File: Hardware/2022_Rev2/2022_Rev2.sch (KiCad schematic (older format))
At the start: 36 parts

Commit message: molex pins
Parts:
- added Conn? (x2): Molex_SL_10, symbol MRDT_Connectors:Molex_SL_10
- added Conn? (x2): Molex_SL_02, symbol MRDT_Connectors:Molex_SL_02
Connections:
- net labels added: TeensyMolexPins
- net labels removed: Teensy
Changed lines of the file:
@@
 $Descr A4 11693 8268
 encoding utf-8
-Sheet 1 5
+Sheet 1 4
 Title ""
 Date ""
@@
 	1    0    0    -1
 $EndComp
-Text GLabel 2000 1050 0    50   Input ~ 0
-Current_Sense_Drive
-Text GLabel 2000 1450 0    50   Input ~ 0
-Current_Sense_Nav
-Wire Wire Line
-	2000 1050 2150 1050
-Wire Wire Line
-	2150 1450 2000 1450
-Text GLabel 4600 1050 2    50   Output ~ 0
-Driver_Drive
-Wire Wire Line
-	4450 1050 4600 1050
-Text GLabel 4600 1450 2    50   Output ~ 0
-Driver_Nav
-Wire Wire Line
-	4450 1450 4600 1450
 Wire Notes Line
 	500  500  5350 500
 Text Label 450  2500 0    315  Italic 63
-Teensy
+TeensyMolexPins
 Wire Notes Line
 	500  2500 5350 2500
@@
 Text Label 7100 7050 0    157  Italic 31
 "Rev4"
-$Sheet
-S 2150 600  2300 1800
-U 62118F7B
-F0 "TEENSY" 50
-F1 "TEENSY.sch" 50
-F2 "Current_Sense_Drive" I L 2150 1050 50
-F3 "Current_Sense_Nav" I L 2150 1450 50
-F4 "Driver_Drive" O R 4450 1050 50
-F5 "Driver_Nav" O R 4450 1450 50
-F6 "Current_Sense_BBB" I L 2150 750 50
-F7 "Current_Sense_Multi" I L 2150 1350 50
-F8 "Current_Sense_Cam2" I L 2150 950 50
-F9 "Current_Sense_Cam1" I L 2150 850 50
-F10 "Driver_BBB" O R 4450 750 50
-F11 "Driver_Multi" O R 4450 1350 50
-F12 "Driver_GimAct" O R 4450 1150 50
-F13 "Driver_Cam1" O R 4450 850 50
-F14 "Driver_Cam2" O R 4450 950 50
-F15 "Current_Sense_GimAct" I L 2150 1150 50
-F16 "Driver_GimLog" O R 4450 1250 50
-F17 "Driver_NetSwitch" O R 4450 1550 50
-F18 "Driver_AuxLog" O R 4450 650 50
-F19 "Driver_SciLog" O R 4450 1750 50
-F20 "Driver_SciAct" O R 4450 1650 50
-F21 "Current_Sense_GimLog" I L 2150 1250 50
-F22 "Current_Sense_NetSwitch" I L 2150 1550 50
-F23 "Current_Sense_SciAct" I L 2150 1650 50
-F24 "Current_Sense_SciLog" I L 2150 1750 50
-F25 "Current_Sense_AuxLog" I L 2150 650 50
-$EndSheet
-Text GLabel 2000 650  0    50   Input ~ 0
-Current_Sense_AuxLog
-Wire Wire Line
-	2000 650  2150 650
-Text GLabel 2000 750  0    50   Input ~ 0
-Current_Sense_BBB
-Wire Wire Line
-	2000 750  2150 750
-Text GLabel 2000 850  0    50   Input ~ 0
-Current_Sense_Cam1
-Wire Wire Line
-	2000 850  2150 850
-Text GLabel 2000 950  0    50   Input ~ 0
-Current_Sense_Cam2
-Wire Wire Line
-	2000 950  2150 950
-Text GLabel 2000 1150 0    50   Input ~ 0
-Current_Sense_GimAct
-Wire Wire Line
-	2000 1150 2150 1150
-Text GLabel 2000 1250 0    50   Input ~ 0
-Current_Sense_GimLog
-Wire Wire Line
-	2000 1250 2150 1250
-Text GLabel 2000 1350 0    50   Input ~ 0
-Current_Sense_Multi
-Wire Wire Line
-	2000 1350 2150 1350
-Text GLabel 2000 1550 0    50   Input ~ 0
-Current_Sense_NetSwitch
-Wire Wire Line
-	2000 1550 2150 1550
-Text GLabel 2000 1650 0    50   Input ~ 0
-Current_Sense_SciAct
-Wire Wire Line
-	2000 1650 2150 1650
-Text GLabel 2000 1750 0    50   Input ~ 0
-Current_Sense_SciLog
-Wire Wire Line
-	2000 1750 2150 1750
-Text GLabel 4600 650  2    50   Output ~ 0
-Driver_AuxLog
-Wire Wire Line
-	4450 650  4600 650
-Text GLabel 4600 750  2    50   Output ~ 0
-Driver_BBB
-Wire Wire Line
-	4450 750  4600 750
-Text GLabel 4600 850  2    50   Output ~ 0
-Driver_Cam1
-Wire Wire Line
-	4450 850  4600 850
-Text GLabel 4600 950  2    50   Output ~ 0
-Driver_Cam2
-Wire Wire Line
-	4450 950  4600 950
-Text GLabel 4600 1150 2    50   Output ~ 0
-Driver_GimAct
-Wire Wire Line
-	4450 1150 4600 1150
-Text GLabel 4600 1250 2    50   Output ~ 0
-Driver_GimLog
-Wire Wire Line
-	4450 1250 4600 1250
-Text GLabel 4600 1350 2    50   Output ~ 0
-Driver_Multi
-Wire Wire Line
-	4450 1350 4600 1350
-Text GLabel 4600 1550 2    50   Output ~ 0
-Driver_NetSwitch
-Wire Wire Line
-	4450 1550 4600 1550
-Text GLabel 4600 1650 2    50   Output ~ 0
-Driver_SciAct
-Wire Wire Line
-	4450 1650 4600 1650
-Text GLabel 4600 1750 2    50   Output ~ 0
-Driver_SciLog
-Wire Wire Line
-	4450 1750 4600 1750
 Text GLabel 5950 1500 0    50   Input ~ 0
 Driver_Drive
@@
 Connection ~ 10150 6500
 Connection ~ 10400 6500
+$Comp
+L MRDT_Connectors:Molex_SL_10 Conn?
+U 1 1 622C6D4E
+P 2300 1550
+F 0 "Conn?" H 2428 2108 60  0000 L CNN
+F 1 "Molex_SL_10" H 2428 2002 60  0000 L CNN
+F 2 "" H 2300 2050 60  0001 C CNN
+F 3 "" H 2300 2050 60  0001 C CNN
+	1    2300 1550
+	1    0    0    -1
+$EndComp
+$Comp
+L MRDT_Connectors:Molex_SL_02 Conn?
+U 1 1 622C7AC7
+P 2300 1750
+F 0 "Conn?" H 2428 1908 60  0000 L CNN
+F 1 "Molex_SL_02" H 2428 1802 60  0000 L CNN
+F 2 "" H 2300 1650 60  0001 C CNN
+F 3 "" H 2300 1650 60  0001 C CNN
+	1    2300 1750
+	1    0    0    -1
+$EndComp
+$Comp
+L MRDT_Connectors:Molex_SL_10 Conn?
+U 1 1 622C9F32
+P 3800 1550
+F 0 "Conn?" H 3928 2108 60  0000 L CNN
+F 1 "Molex_SL_10" H 3928 2002 60  0000 L CNN
+F 2 "" H 3800 2050 60  0001 C CNN
+F 3 "" H 3800 2050 60  0001 C CNN
+	1    3800 1550
+	-1   0    0    -1
+$EndComp
+$Comp
+L MRDT_Connectors:Molex_SL_02 Conn?
+U 1 1 622C9F38
+P 3800 1750
+F 0 "Conn?" H 3928 1908 60  0000 L CNN
+F 1 "Molex_SL_02" H 3928 1802 60  0000 L CNN
+F 2 "" H 3800 1650 60  0001 C CNN
+F 3 "" H 3800 1650 60  0001 C CNN
+	1    3800 1750
+	-1   0    0    -1
+$EndComp
+Text GLabel 1950 1000 0    50   Input ~ 0
+Current_Sense_Drive
+Text GLabel 1950 1400 0    50   Input ~ 0
+Current_Sense_Nav
+Wire Wire Line
+	1950 1000 2100 1000
+Wire Wire Line
+	2100 1400 1950 1400
+Text GLabel 1950 600  0    50   Input ~ 0
+Current_Sense_AuxLog
+Wire Wire Line
+	1950 600  2100 600
+Text GLabel 1950 700  0    50   Input ~ 0
+Current_Sense_BBB
+Wire Wire Line
+	1950 700  2100 700
+Text GLabel 1950 800  0    50   Input ~ 0
+Current_Sense_Cam1
+Wire Wire Line
+	1950 800  2100 800
+Text GLabel 1950 900  0    50   Input ~ 0
+Current_Sense_Cam2
+Wire Wire Line
+	1950 900  2100 900
+Text GLabel 1950 1100 0    50   Input ~ 0
+Current_Sense_GimAct
+Wire Wire Line
+	1950 1100 2100 1100
+Text GLabel 1950 1200 0    50   Input ~ 0
+Current_Sense_GimLog
+Wire Wire Line
+	1950 1200 2100 1200
+Text GLabel 1950 1300 0    50   Input ~ 0
+Current_Sense_Multi
+Wire Wire Line
+	1950 1300 2100 1300
+Text GLabel 1950 1500 0    50   Input ~ 0
+Current_Sense_NetSwitch
+Wire Wire Line
+	1950 1500 2100 1500
+Text GLabel 1950 1600 0    50   Input ~ 0
+Current_Sense_SciAct
+Wire Wire Line
+	1950 1600 2100 1600
+Text GLabel 1950 1700 0    50   Input ~ 0
+Current_Sense_SciLog
+Wire Wire Line
+	1950 1700 2100 1700
+Text GLabel 4150 1000 2    50   Output ~ 0
+Driver_Drive
+Wire Wire Line
+	4000 1000 4150 1000
+Text GLabel 4150 1400 2    50   Output ~ 0
+Driver_Nav
+Wire Wire Line
+	4000 1400 4150 1400
+Text GLabel 4150 600  2    50   Output ~ 0
+Driver_AuxLog
+Wire Wire Line
+	4000 600  4150 600
+Text GLabel 4150 700  2    50   Output ~ 0
+Driver_BBB
+Wire Wire Line
+	4000 700  4150 700
+Text GLabel 4150 800  2    50   Output ~ 0
+Driver_Cam1
+Wire Wire Line
+	4000 800  4150 800
+Text GLabel 4150 900  2    50   Output ~ 0
+Driver_Cam2
+Wire Wire Line
+	4000 900  4150 900
+Text GLabel 4150 1100 2    50   Output ~ 0
+Driver_GimAct
+Wire Wire Line
+	4000 1100 4150 1100
+Text GLabel 4150 1200 2    50   Output ~ 0
+Driver_GimLog
+Wire Wire Line
+	4000 1200 4150 1200
+Text GLabel 4150 1300 2    50   Output ~ 0
+Driver_Multi
+Wire Wire Line
+	4000 1300 4150 1300
+Text GLabel 4150 1500 2    50   Output ~ 0
+Driver_NetSwitch
+Wire Wire Line
+	4000 1500 4150 1500
+Text GLabel 4150 1600 2    50   Output ~ 0
+Driver_SciAct
+Wire Wire Line
+	4000 1600 4150 1600
+Text GLabel 4150 1700 2    50   Output ~ 0
+Driver_SciLog
+Wire Wire Line
+	4000 1700 4150 1700
 $EndSCHEMATC

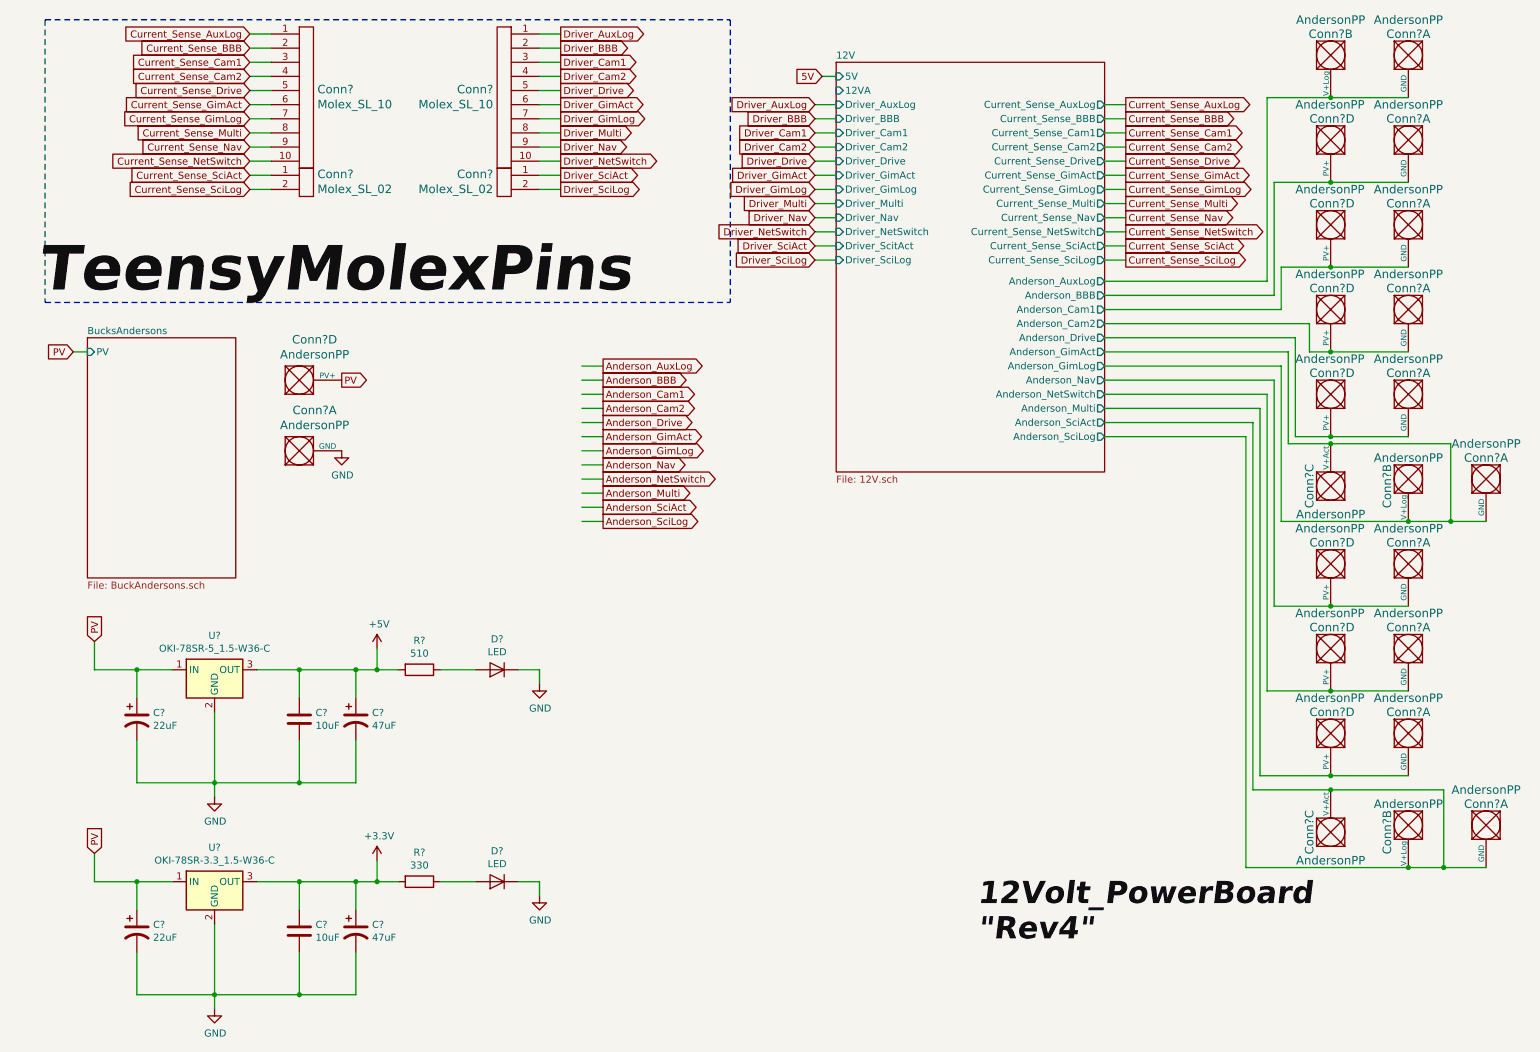
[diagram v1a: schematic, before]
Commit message: removed scilog/sciact
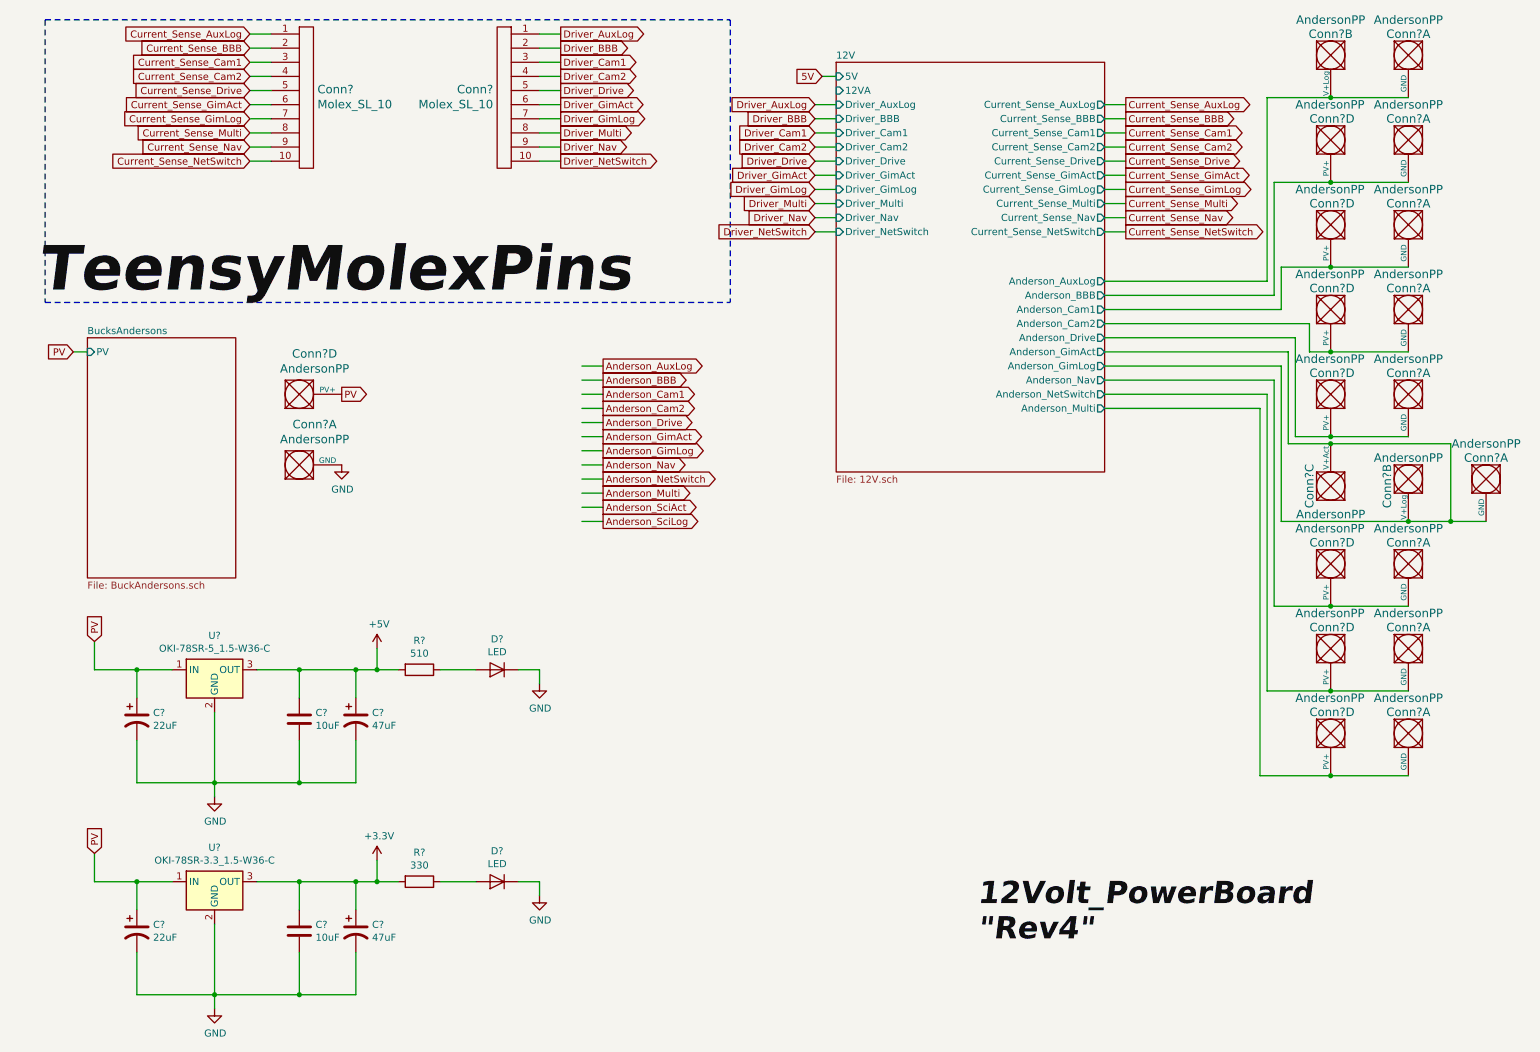
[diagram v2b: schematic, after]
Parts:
- removed Conn? (x2): Molex_SL_02, symbol MRDT_Connectors:Molex_SL_02
- removed Conn? (x3): AndersonPP, symbol MRDT_Connectors:AndersonPP
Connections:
- net labels removed: Current_Sense_SciAct, Current_Sense_SciLog, Driver_SciAct, Driver_SciLog
- wire segments 158 -> 140
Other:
- moved on the sheet: Conn?A, Conn?D
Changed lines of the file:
@@
 L 2022_Rev2-rescue:AndersonPP-MRDT_Connectors Conn?
 U 4 1 62120188
-P 2200 3150
+P 2200 3250
 AR Path="/62118E70/62120188" Ref="Conn?"  Part="4"
 AR Path="/62120188" Ref="Conn?"  Part="4"
-F 0 "Conn?" H 2408 3537 60  0000 C CNN
-F 1 "AndersonPP" H 2408 3431 60  0000 C CNN
-F 2 "" H 2050 2600 60  0001 C CNN
-F 3 "" H 2050 2600 60  0001 C CNN
-	4    2200 3150
+F 0 "Conn?" H 2408 3637 60  0000 C CNN
+F 1 "AndersonPP" H 2408 3531 60  0000 C CNN
+F 2 "" H 2050 2700 60  0001 C CNN
+F 3 "" H 2050 2700 60  0001 C CNN
+	4    2200 3250
 	1    0    0    -1
 $EndComp
@@
 L 2022_Rev2-rescue:AndersonPP-MRDT_Connectors Conn?
 U 1 1 6212018E
-P 2200 3650
+P 2200 3750
 AR Path="/62118E70/6212018E" Ref="Conn?"  Part="1"
 AR Path="/6212018E" Ref="Conn?"  Part="1"
-F 0 "Conn?" H 2408 4037 60  0000 C CNN
-F 1 "AndersonPP" H 2408 3931 60  0000 C CNN
-F 2 "" H 2050 3100 60  0001 C CNN
-F 3 "" H 2050 3100 60  0001 C CNN
-	1    2200 3650
+F 0 "Conn?" H 2408 4137 60  0000 C CNN
+F 1 "AndersonPP" H 2408 4031 60  0000 C CNN
+F 2 "" H 2050 3200 60  0001 C CNN
+F 3 "" H 2050 3200 60  0001 C CNN
+	1    2200 3750
 	1    0    0    -1
 $EndComp
@@
 L power:GND #PWR?
 U 1 1 62120194
-P 2600 3550
+P 2600 3650
 AR Path="/62118E70/62120194" Ref="#PWR?"  Part="1"
 AR Path="/62120194" Ref="#PWR?"  Part="1"
-F 0 "#PWR?" H 2600 3300 50  0001 C CNN
-F 1 "GND" H 2605 3377 50  0000 C CNN
-F 2 "" H 2600 3550 50  0001 C CNN
-F 3 "" H 2600 3550 50  0001 C CNN
-	1    2600 3550
-	1    0    0    -1
-$EndComp
-Text GLabel 2600 3050 2    50   Output ~ 0
+F 0 "#PWR?" H 2600 3400 50  0001 C CNN
+F 1 "GND" H 2605 3477 50  0000 C CNN
+F 2 "" H 2600 3650 50  0001 C CNN
+F 3 "" H 2600 3650 50  0001 C CNN
+	1    2600 3650
+	1    0    0    -1
+$EndComp
+Text GLabel 2600 3150 2    50   Output ~ 0
 PV
 Text GLabel 850  4900 1    50   Input ~ 0
@@
 Wire Wire Line
 	6100 2000 5950 2000
-Text GLabel 5950 2100 0    50   Input ~ 0
-Driver_SciAct
-Wire Wire Line
-	6100 2100 5950 2100
-Text GLabel 5950 2200 0    50   Input ~ 0
-Driver_SciLog
-Wire Wire Line
-	6100 2200 5950 2200
 Text GLabel 8150 1500 2    50   Output ~ 0
 Current_Sense_Drive
@@
 Wire Wire Line
 	8150 2000 8000 2000
-Text GLabel 8150 2100 2    50   Output ~ 0
-Current_Sense_SciAct
-Wire Wire Line
-	8150 2100 8000 2100
-Text GLabel 8150 2200 2    50   Output ~ 0
-Current_Sense_SciLog
-Wire Wire Line
-	8150 2200 8000 2200
 Text GLabel 4450 2950 2    50   Output ~ 0
 Anderson_AuxLog
@@
 Wire Wire Line
 	4450 3850 4300 3850
-Text GLabel 4450 3950 2    50   Output ~ 0
-Anderson_SciAct
-Wire Wire Line
-	4450 3950 4300 3950
-Text GLabel 4450 4050 2    50   Output ~ 0
-Anderson_SciLog
-Wire Wire Line
-	4450 4050 4300 4050
 $Comp
 L MRDT_Connectors:AndersonPP Conn?
@@
 F9 "Anderson_GimAct" O R 8000 2850 50
 F10 "Driver_GimAct" I L 6100 1600 50
-F11 "Current_Sense_SciAct" O R 8000 2100 50
-F12 "Anderson_SciAct" O R 8000 3350 50
-F13 "Driver_ScitAct" I L 6100 2100 50
-F14 "Current_Sense_Cam1" O R 8000 1300 50
-F15 "Current_Sense_Cam2" O R 8000 1400 50
-F16 "Current_Sense_GimLog" O R 8000 1700 50
-F17 "Current_Sense_Multi" O R 8000 1800 50
-F18 "Current_Sense_NetSwitch" O R 8000 2000 50
-F19 "Current_Sense_SciLog" O R 8000 2200 50
-F20 "Anderson_BBB" O R 8000 2450 50
-F21 "Anderson_Cam1" O R 8000 2550 50
-F22 "Anderson_Cam2" O R 8000 2650 50
-F23 "Anderson_GimLog" O R 8000 2950 50
-F24 "Anderson_Multi" O R 8000 3250 50
-F25 "Anderson_Nav" O R 8000 3050 50
-F26 "Anderson_NetSwitch" O R 8000 3150 50
-F27 "Anderson_SciLog" O R 8000 3450 50
-F28 "Driver_BBB" I L 6100 1200 50
-F29 "Driver_Cam1" I L 6100 1300 50
-F30 "Driver_Cam2" I L 6100 1400 50
-F31 "Driver_GimLog" I L 6100 1700 50
-F32 "Driver_Multi" I L 6100 1800 50
-F33 "Driver_NetSwitch" I L 6100 2000 50
-F34 "Driver_SciLog" I L 6100 2200 50
-F35 "12VA" I L 6100 1000 50
-F36 "Current_Sense_AuxLog" O R 8000 1100 50
-F37 "Current_Sense_BBB" O R 8000 1200 50
-F38 "Anderson_AuxLog" O R 8000 2350 50
-F39 "Driver_AuxLog" I L 6100 1100 50
+F11 "Current_Sense_Cam1" O R 8000 1300 50
+F12 "Current_Sense_Cam2" O R 8000 1400 50
+F13 "Current_Sense_GimLog" O R 8000 1700 50
+F14 "Current_Sense_Multi" O R 8000 1800 50
+F15 "Current_Sense_NetSwitch" O R 8000 2000 50
+F16 "Anderson_BBB" O R 8000 2450 50
+F17 "Anderson_Cam1" O R 8000 2550 50
+F18 "Anderson_Cam2" O R 8000 2650 50
+F19 "Anderson_GimLog" O R 8000 2950 50
+F20 "Anderson_Multi" O R 8000 3250 50
+F21 "Anderson_Nav" O R 8000 3050 50
+F22 "Anderson_NetSwitch" O R 8000 3150 50
+F23 "Driver_BBB" I L 6100 1200 50
+F24 "Driver_Cam1" I L 6100 1300 50
+F25 "Driver_Cam2" I L 6100 1400 50
+F26 "Driver_GimLog" I L 6100 1700 50
+F27 "Driver_Multi" I L 6100 1800 50
+F28 "Driver_NetSwitch" I L 6100 2000 50
+F29 "12VA" I L 6100 1000 50
+F30 "Current_Sense_AuxLog" O R 8000 1100 50
+F31 "Current_Sense_BBB" O R 8000 1200 50
+F32 "Anderson_AuxLog" O R 8000 2350 50
+F33 "Driver_AuxLog" I L 6100 1100 50
 $EndSheet
 Wire Wire Line
@@
 Connection ~ 10150 4050
 Connection ~ 10450 4050
-$Comp
-L MRDT_Connectors:AndersonPP Conn?
-U 1 1 626D966C
-P 10600 6100
-F 0 "Conn?" V 10550 6200 60  0000 C CNN
-F 1 "AndersonPP" V 10450 6200 60  0000 C CNN
-F 2 "" H 10450 5550 60  0001 C CNN
-F 3 "" H 10450 5550 60  0001 C CNN
-	1    10600 6100
-	0    1    1    0
-$EndComp
-$Comp
-L MRDT_Connectors:AndersonPP Conn?
-U 3 1 626D9672
-P 9700 6350
-F 0 "Conn?" H 9800 6600 60  0000 C CNN
-F 1 "AndersonPP" V 9600 6450 60  0000 C CNN
-F 2 "" H 9550 5800 60  0001 C CNN
-F 3 "" H 9550 5800 60  0001 C CNN
-	3    9700 6350
-	0    -1   -1   0
-$EndComp
-$Comp
-L MRDT_Connectors:AndersonPP Conn?
-U 2 1 626D9678
-P 10050 6100
-F 0 "Conn?" H 10200 6050 60  0000 C CNN
-F 1 "AndersonPP" V 10000 6200 60  0000 C CNN
-F 2 "" H 9900 5550 60  0001 C CNN
-F 3 "" H 9900 5550 60  0001 C CNN
-	2    10050 6100
-	0    1    1    0
-$EndComp
 Wire Wire Line
 	8000 3050 9200 3050
@@
 Wire Wire Line
 	9600 5850 10150 5850
-Wire Wire Line
-	8000 3350 9050 3350
-Wire Wire Line
-	9050 3350 9050 5950
-Wire Wire Line
-	9050 5950 9600 5950
-Wire Wire Line
-	8000 3450 9000 3450
-Wire Wire Line
-	9000 3450 9000 6500
-Wire Wire Line
-	9000 6500 10150 6500
-Wire Wire Line
-	9600 5950 10400 5950
-Wire Wire Line
-	10400 5950 10400 6500
-Wire Wire Line
-	10400 6500 10700 6500
-Connection ~ 9600 5950
-Wire Wire Line
-	10150 6500 10400 6500
-Connection ~ 10150 6500
-Connection ~ 10400 6500
 $Comp
 L MRDT_Connectors:Molex_SL_10 Conn?
@@
 F 3 "" H 2300 2050 60  0001 C CNN
 	1    2300 1550
-	1    0    0    -1
-$EndComp
-$Comp
-L MRDT_Connectors:Molex_SL_02 Conn?
-U 1 1 622C7AC7
-P 2300 1750
-F 0 "Conn?" H 2428 1908 60  0000 L CNN
-F 1 "Molex_SL_02" H 2428 1802 60  0000 L CNN
-F 2 "" H 2300 1650 60  0001 C CNN
-F 3 "" H 2300 1650 60  0001 C CNN
-	1    2300 1750
 	1    0    0    -1
 $EndComp
@@
 	-1   0    0    -1
 $EndComp
-$Comp
-L MRDT_Connectors:Molex_SL_02 Conn?
-U 1 1 622C9F38
-P 3800 1750
-F 0 "Conn?" H 3928 1908 60  0000 L CNN
-F 1 "Molex_SL_02" H 3928 1802 60  0000 L CNN
-F 2 "" H 3800 1650 60  0001 C CNN
-F 3 "" H 3800 1650 60  0001 C CNN
-	1    3800 1750
-	-1   0    0    -1
-$EndComp
 Text GLabel 1950 1000 0    50   Input ~ 0
 Current_Sense_Drive
@@
 Wire Wire Line
 	1950 1500 2100 1500
-Text GLabel 1950 1600 0    50   Input ~ 0
-Current_Sense_SciAct
-Wire Wire Line
-	1950 1600 2100 1600
-Text GLabel 1950 1700 0    50   Input ~ 0
-Current_Sense_SciLog
-Wire Wire Line
-	1950 1700 2100 1700
 Text GLabel 4150 1000 2    50   Output ~ 0
 Driver_Drive
@@
 Wire Wire Line
 	4000 1500 4150 1500
-Text GLabel 4150 1600 2    50   Output ~ 0
-Driver_SciAct
-Wire Wire Line
-	4000 1600 4150 1600
-Text GLabel 4150 1700 2    50   Output ~ 0
-Driver_SciLog
-Wire Wire Line
-	4000 1700 4150 1700
+Wire Wire Line
+	4450 4050 4300 4050
+Text GLabel 4450 4050 2    50   Output ~ 0
+Anderson_SciLog
+Wire Wire Line
+	4450 3950 4300 3950
+Text GLabel 4450 3950 2    50   Output ~ 0
+Anderson_SciAct
 $EndSCHEMATC

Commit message: molex pins pt.2
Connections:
- net labels added: 12VA
- wire segments 140 -> 141
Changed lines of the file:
@@
 Text GLabel 4450 3950 2    50   Output ~ 0
 Anderson_SciAct
+Wire Wire Line
+	6100 1000 6000 1000
+Text GLabel 6000 1000 0    50   Input ~ 0
+12VA
 $EndSCHEMATC
